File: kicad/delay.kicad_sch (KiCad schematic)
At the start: 59 parts, among them Q3 2N3904, U3 4020, U4 TL072, U5 TL074, U6 PT2399

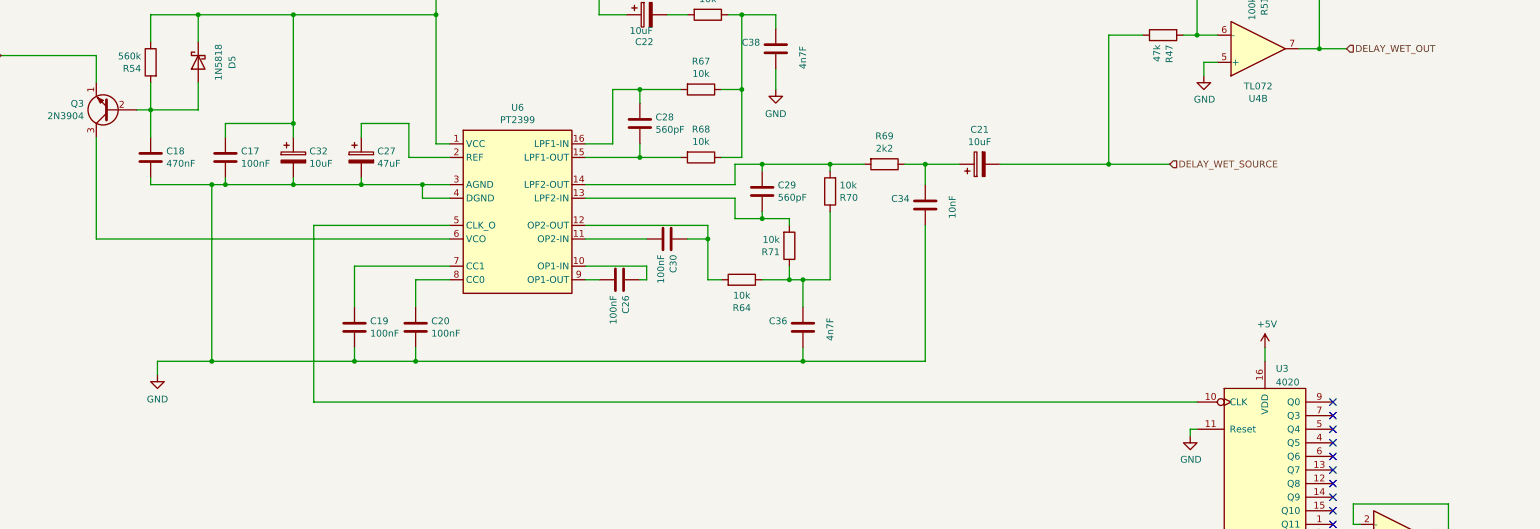
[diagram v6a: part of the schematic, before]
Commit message: Updating with rev03 changes
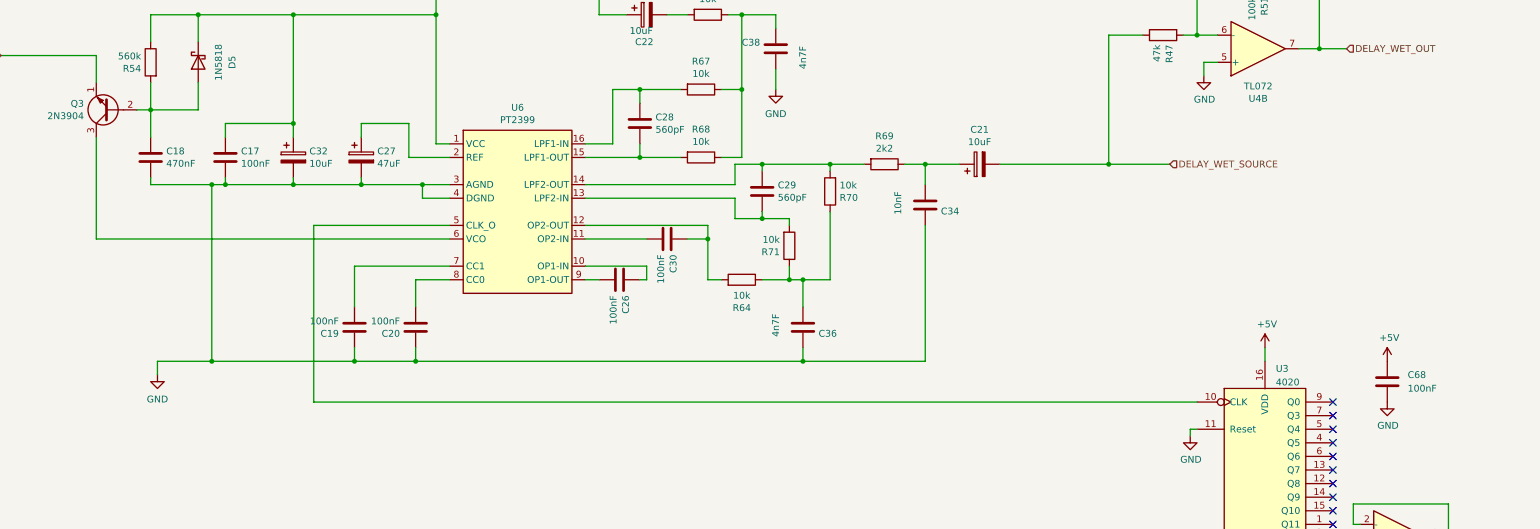
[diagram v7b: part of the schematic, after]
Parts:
- added C68: 100nF, Rumblesan_Standard_Parts:C_Rect_L7.0mm_W2.5mm_P5.00mm, symbol Rumblesan_Standard_Parts:C
- C19, C20, C26, C28, C29, C30, C36, C38: footprint Rumblesan_Standard_Parts:C_Rect_L7.0mm_W3.5mm_P5.00mm -> Rumblesan_Standard_Parts:C_Rect_L7.0mm_W2.5mm_P5.00mm
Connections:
- net +5V: now also C68.1
- net GND: now also C19.2, C20.2, C34.2, C36.2, C68.2; no longer C19.1, C20.1, C34.1, C36.1
- net at R64.2, R70.2, R71.2: now also C36.1; no longer C36.2
- net at U6.7 (CC1): now also C19.1; no longer C19.2
- net at U6.8 (CC0): now also C20.1; no longer C20.2
- net at C21.1, R69.2: now also C34.1; no longer C34.2
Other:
- moved on the sheet: C19, C20

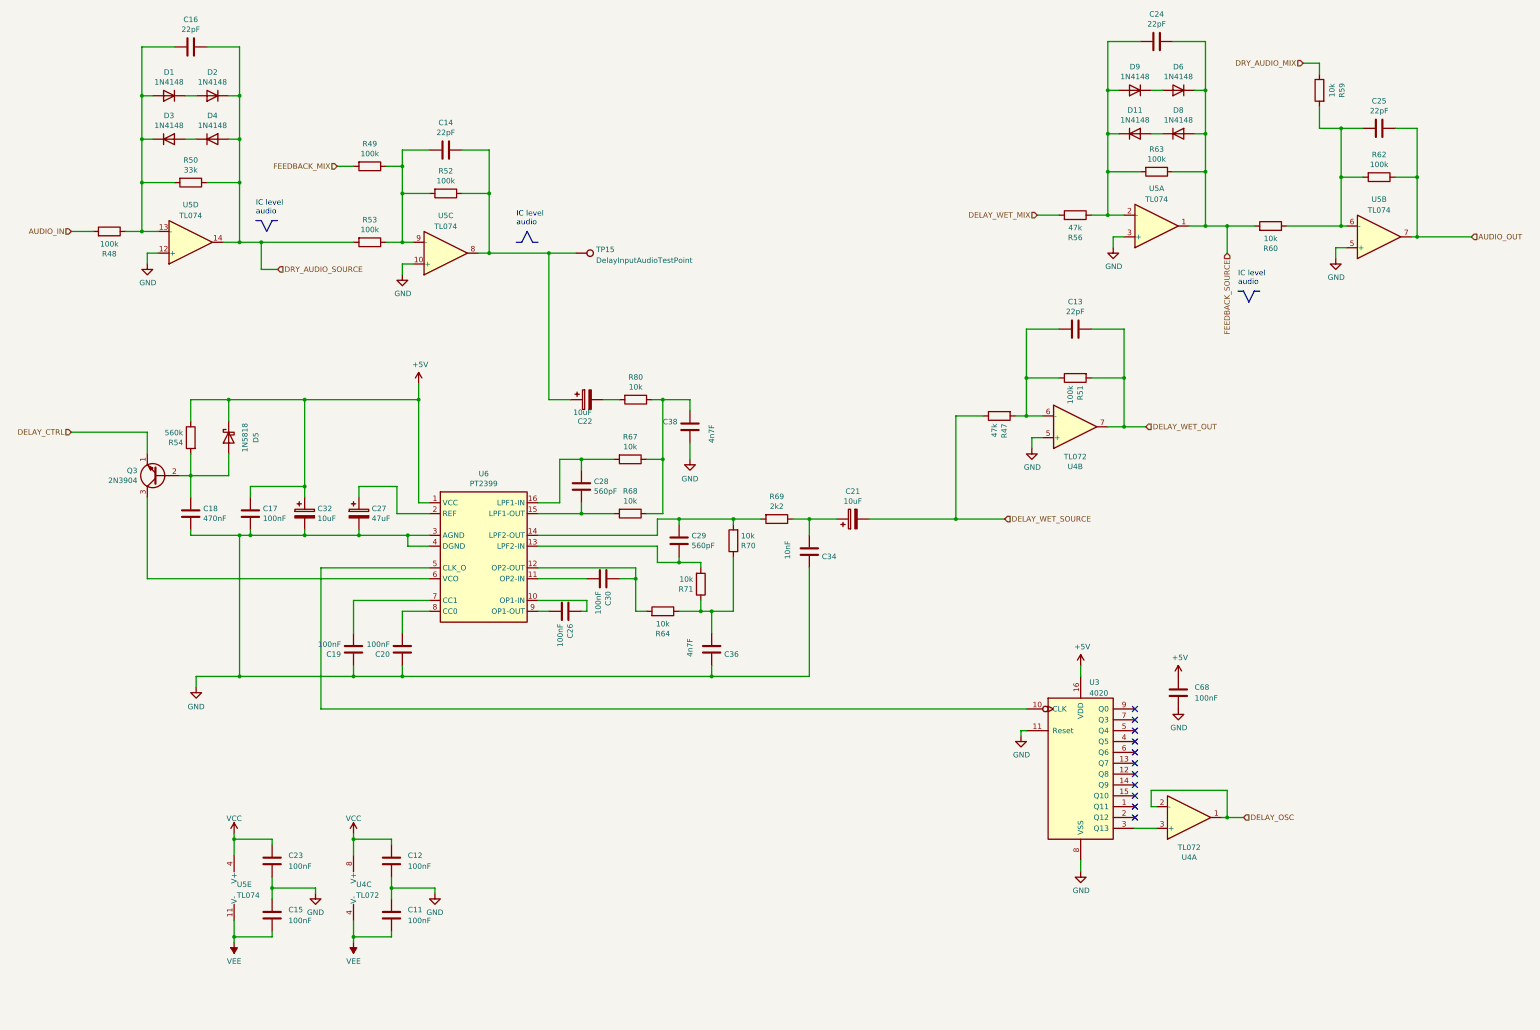
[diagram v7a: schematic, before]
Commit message: Digital ground for divider and other layout improvements
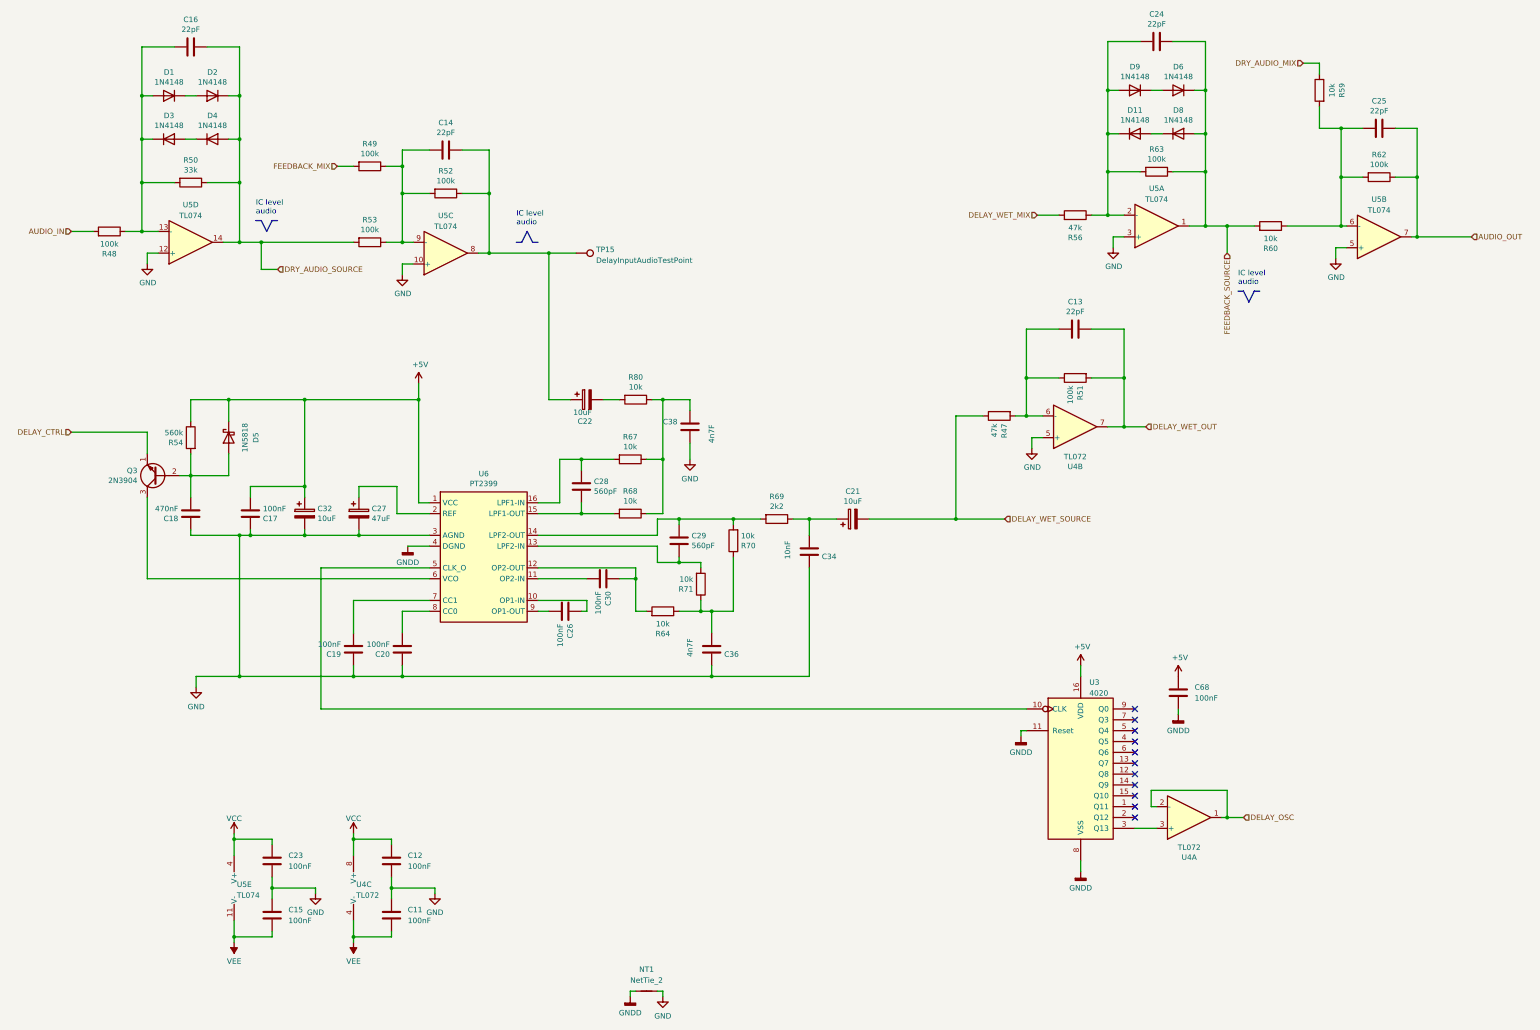
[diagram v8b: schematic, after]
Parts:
- added NT1: NetTie_2, NetTie:NetTie-2_SMD_Pad2.0mm, symbol Device:NetTie_2
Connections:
- net +5V: now also C17.1; no longer C17.2
- net GND: now also C17.2, C18.1, NT1.2; no longer C17.1, C18.2, C68.2, U3.11 (Reset), U3.8 (VSS), U6.4 (DGND)
- net at D5.2 (A), Q3.2 (B), R54.1: now also C18.2; no longer C18.1
- new net GNDD: C68.2, NT1.1, U3.11 (Reset), U3.8 (VSS), U6.4 (DGND)
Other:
- moved on the sheet: C17, C18
